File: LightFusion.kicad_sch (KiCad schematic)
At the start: 28 parts, among them IC2 ADS1291IPBSR, U1 BMD-350-A-R

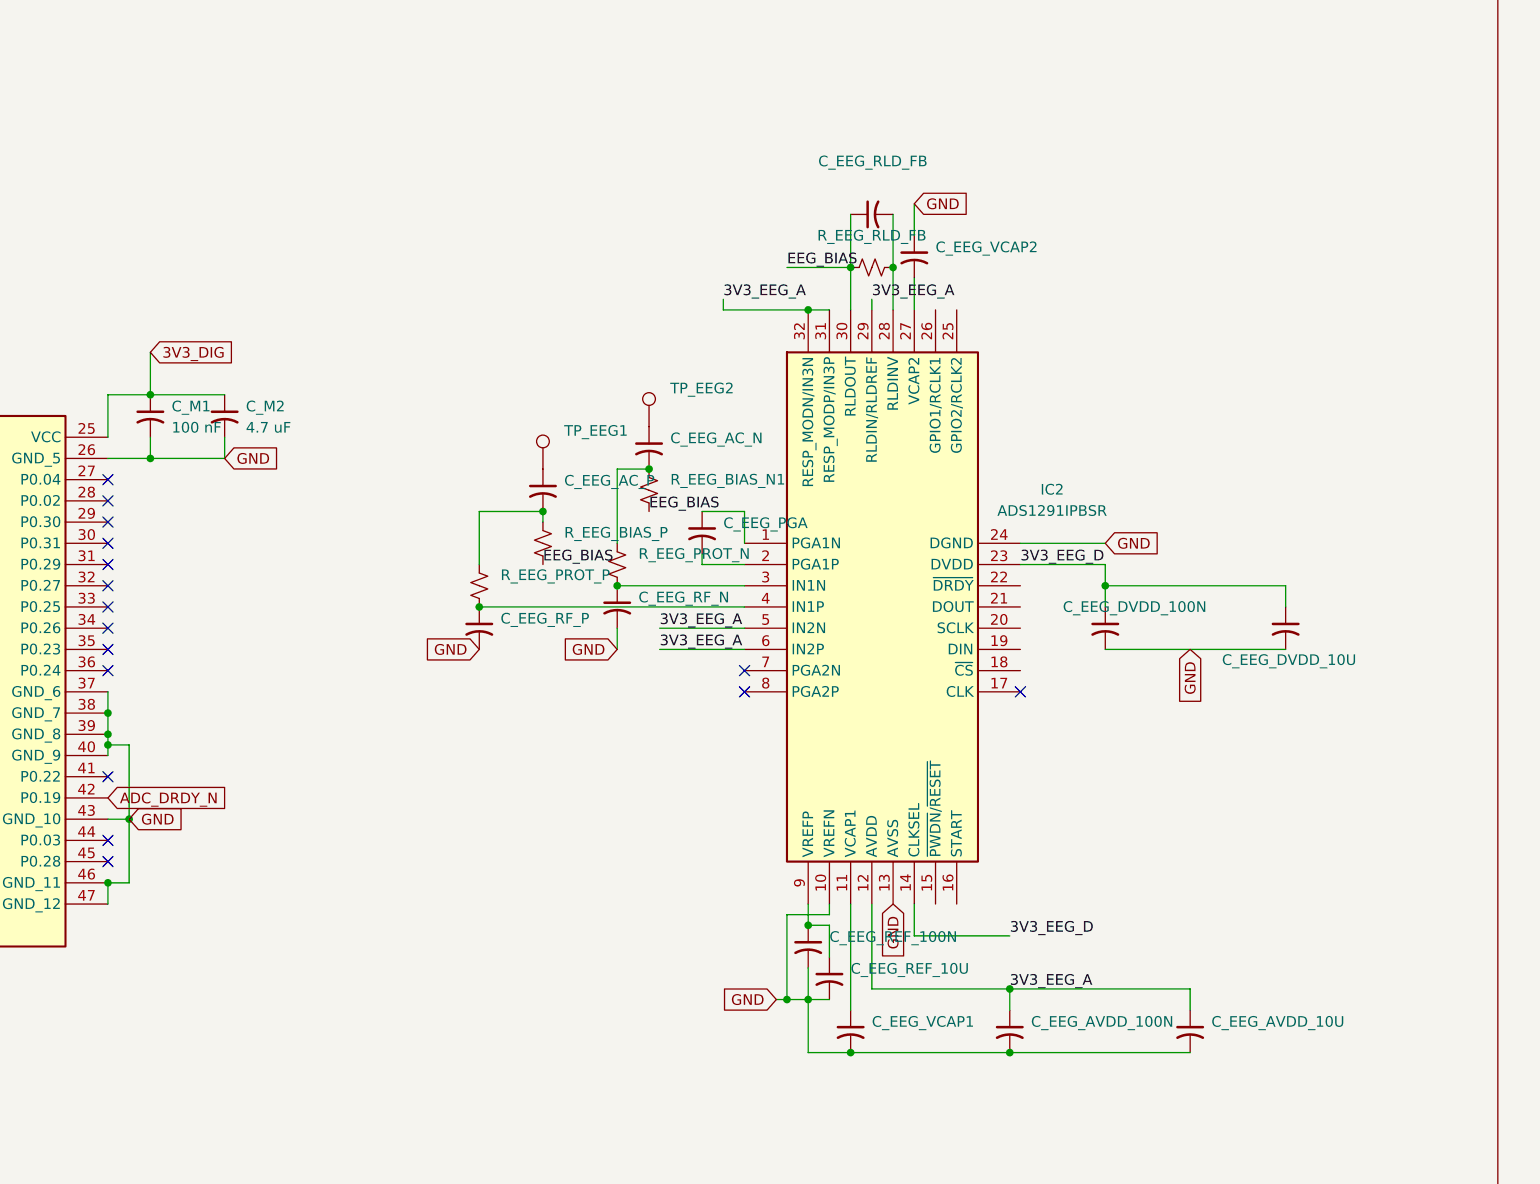
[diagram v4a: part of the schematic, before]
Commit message: eeg part refactored
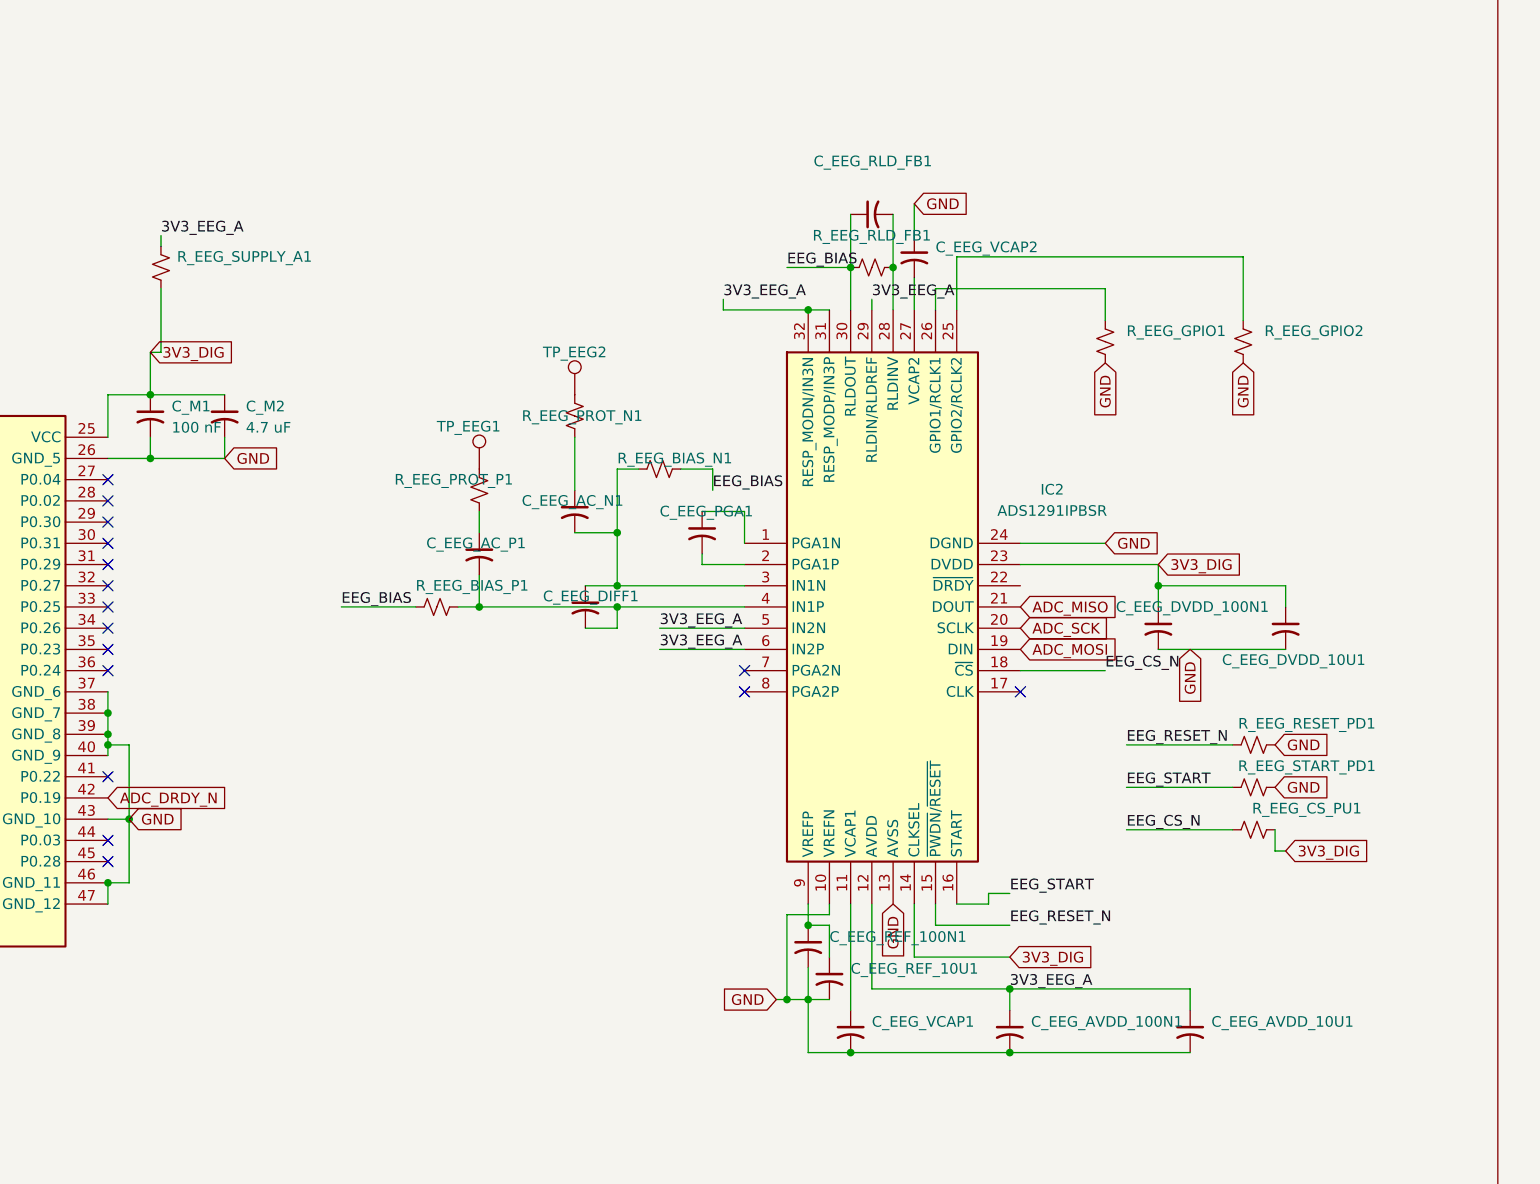
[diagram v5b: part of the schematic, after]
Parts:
- removed C_EEG_RF_P: 47 pF, symbol C_Small_US:C_Small_US
- added R_EEG_CS_PU1, R_EEG_RESET_PD1, R_EEG_START_PD1: 100 kΩ, symbol R_Small_US:R_Small_US
- added R_EEG_GPIO1, R_EEG_GPIO2: 10 kΩ, symbol R_Small_US:R_Small_US
- added R_EEG_SUPPLY_A1: 10 Ω, symbol R_Small_US:R_Small_US
- C_EEG_DIFF1: renamed from C_EEG_RF_N; value 47 pF -> 2.2 nF
- TP_EEG1, TP_EEG2: footprint (none) -> LightFusion:TestPoint_Plated_Hole_D3.0mm
- renumbered C_EEG_AC_N to C_EEG_AC_N1, C_EEG_AC_P to C_EEG_AC_P1, C_EEG_AVDD_100N to C_EEG_AVDD_100N1, C_EEG_AVDD_10U to C_EEG_AVDD_10U1, C_EEG_DVDD_100N to C_EEG_DVDD_100N1, C_EEG_DVDD_10U to C_EEG_DVDD_10U1, C_EEG_PGA to C_EEG_PGA1, C_EEG_REF_100N to C_EEG_REF_100N1, C_EEG_REF_10U to C_EEG_REF_10U1, C_EEG_RLD_FB to C_EEG_RLD_FB1, R_EEG_BIAS_P to R_EEG_BIAS_P1, R_EEG_PROT_N to R_EEG_PROT_N1, R_EEG_PROT_P to R_EEG_PROT_P1, R_EEG_RLD_FB to R_EEG_RLD_FB1
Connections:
- net 3V3_EEG_D is gone; now on net 3V3_DIG: C_EEG_DVDD_100N1.1, C_EEG_DVDD_10U1.1, IC2.14 (CLKSEL), IC2.23 (DVDD)
- net 3V3_DIG: now also R_EEG_CS_PU1.2, R_EEG_SUPPLY_A1.2
- net 3V3_EEG_A: now also R_EEG_SUPPLY_A1.1
- net ADC_MISO: now also IC2.21 (DOUT)
- net ADC_MOSI: now also IC2.19 (DIN)
- net ADC_SCK: now also IC2.20 (SCLK)
- net EEG_BIAS: now also R_EEG_BIAS_N1.1; no longer R_EEG_BIAS_N1.2
- net GND: now also R_EEG_GPIO1.2, R_EEG_GPIO2.2, R_EEG_RESET_PD1.2, R_EEG_START_PD1.2; no longer C_EEG_DIFF1.2
- net at C_EEG_DIFF1.1, IC2.3 (IN1N): now also C_EEG_AC_N1.2, R_EEG_BIAS_N1.2; no longer R_EEG_PROT_N1.2
- net at TP_EEG1.1: now also R_EEG_PROT_P1.1; no longer C_EEG_AC_P1.1
- net at IC2.4 (IN1P): now also C_EEG_AC_P1.2, C_EEG_DIFF1.2, R_EEG_BIAS_P1.1; no longer R_EEG_PROT_P1.2
- net at TP_EEG2.1: now also R_EEG_PROT_N1.1; no longer C_EEG_AC_N1.1
- net EEG_RESET_N: now reaches IC2.15 (~{PWDN}/~{RESET})
- net EEG_RESET_N: now also R_EEG_RESET_PD1.1
- net EEG_START: now reaches IC2.16 (START)
- net EEG_START: now also R_EEG_START_PD1.1
- net EEG_CS_N: now reaches IC2.18 (~{CS})
- net EEG_CS_N: now also R_EEG_CS_PU1.1
- net at IC2.25 (GPIO2/RCLK2): now also R_EEG_GPIO2.1
- net at IC2.26 (GPIO1/RCLK1): now also R_EEG_GPIO1.1
- new net: C_EEG_AC_N1.1, R_EEG_PROT_N1.2
- new net: C_EEG_AC_P1.1, R_EEG_PROT_P1.2
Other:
- moved on the sheet: C_EEG_AC_N1, C_EEG_AC_P1, C_EEG_DIFF1, C_EEG_DVDD_100N1, R_EEG_BIAS_N1, R_EEG_BIAS_P1, R_EEG_PROT_N1, R_EEG_PROT_P1, TP_EEG1, TP_EEG2

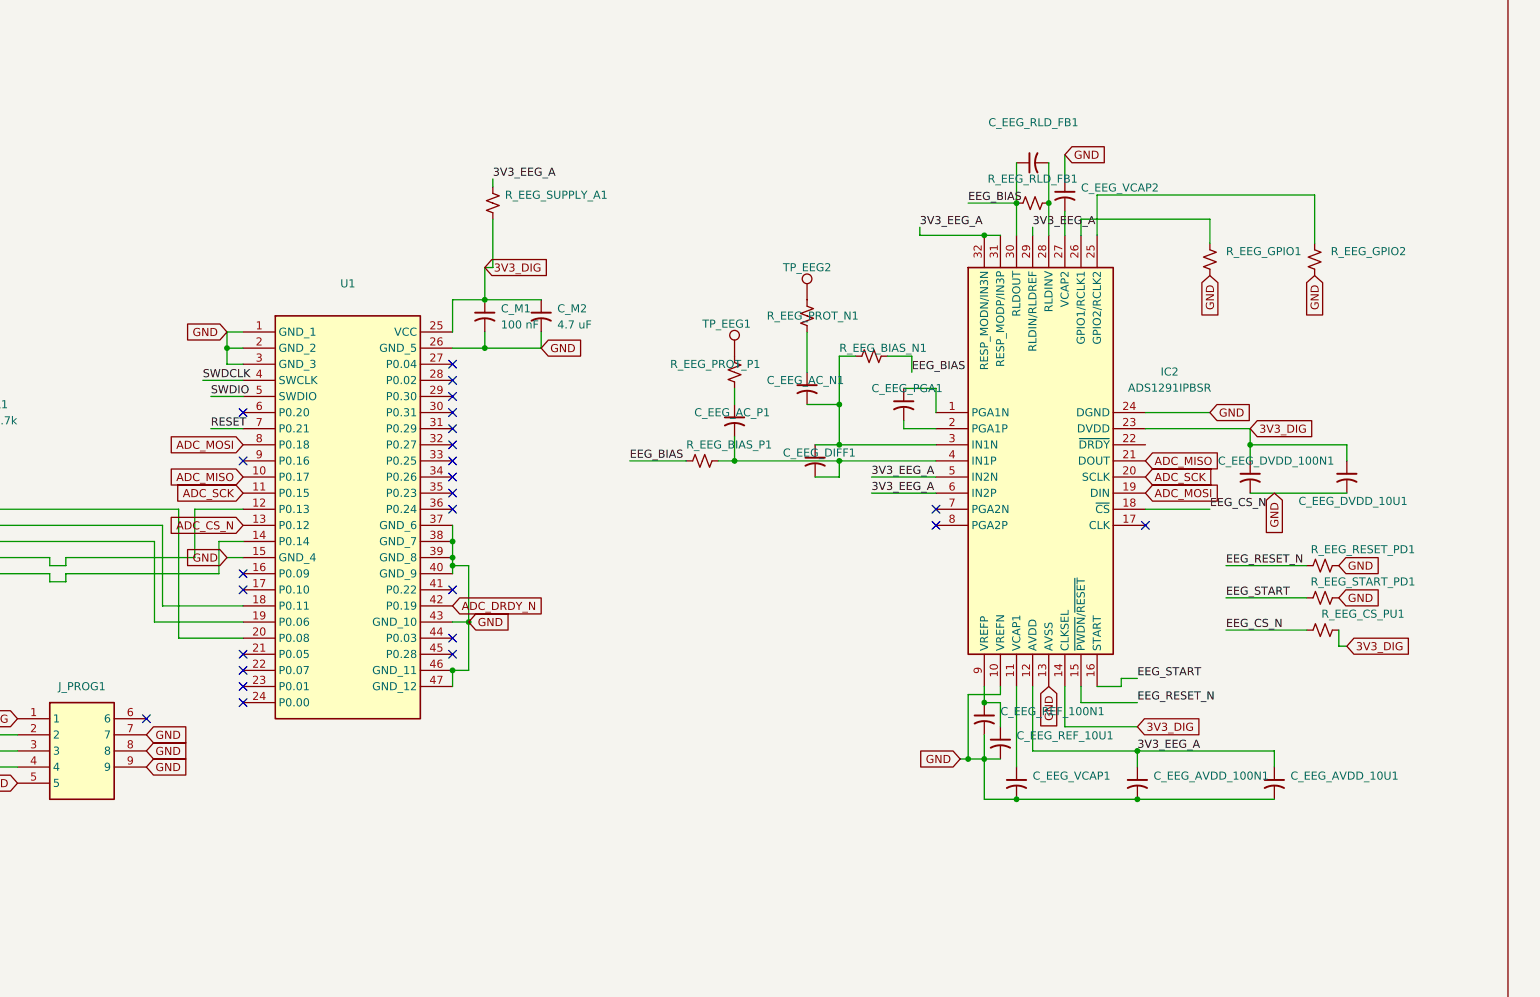
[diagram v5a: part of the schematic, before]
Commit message: eeg part refactored electrodes
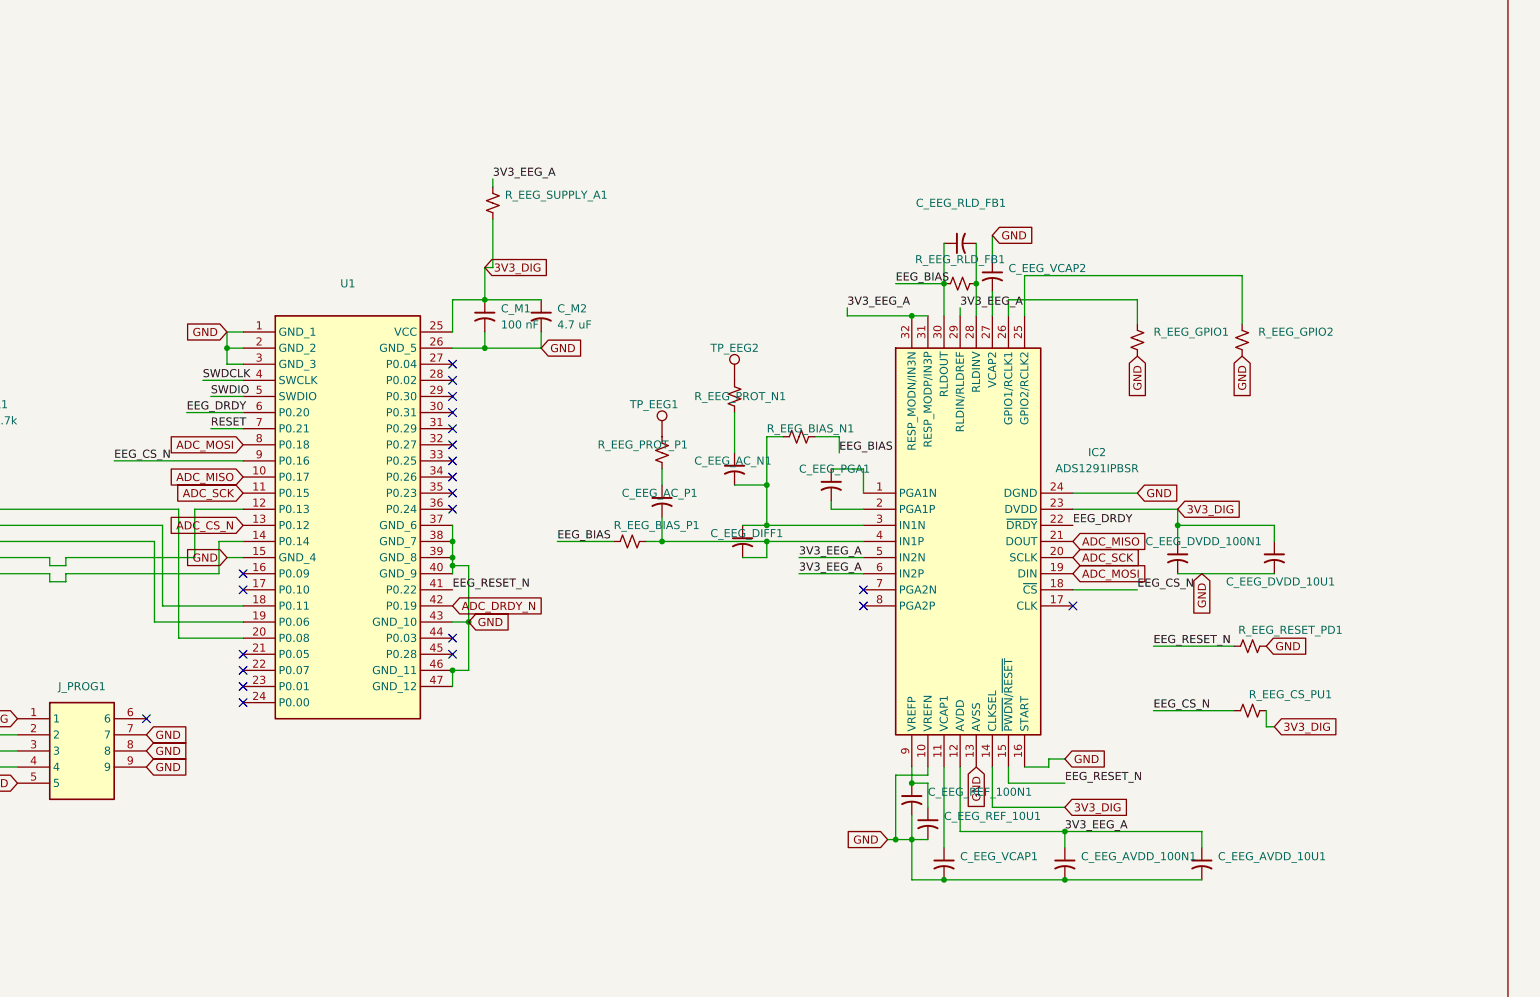
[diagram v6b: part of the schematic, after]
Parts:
- removed R_EEG_START_PD1: 100 kΩ, symbol R_Small_US:R_Small_US
- C_EEG_AC_N1, C_EEG_AC_P1, C_EEG_AVDD_100N1, C_EEG_DVDD_100N1, C_EEG_REF_100N1: footprint (none) -> LightFusion:C_0603_1608Metric
- C_EEG_AVDD_10U1, C_EEG_DVDD_10U1, C_EEG_REF_10U1: footprint (none) -> LightFusion:C_0805_2012Metric
- C_EEG_DIFF1, C_EEG_RLD_FB1: footprint (none) -> LightFusion:C_0402_1005Metric
- C_EEG_VCAP1, C_EEG_VCAP2: footprint (none) -> LightFusion:CAPPC2012X90N
- R_EEG_BIAS_N1, R_EEG_BIAS_P1, R_EEG_CS_PU1, R_EEG_GPIO1, R_EEG_GPIO2, R_EEG_PROT_N1, R_EEG_PROT_P1, R_EEG_RESET_PD1, R_EEG_RLD_FB1, R_EEG_SUPPLY_A1: footprint (none) -> LightFusion:R_0603_1608Metric
- TP_EEG1, TP_EEG2: footprint LightFusion:TestPoint_Plated_Hole_D3.0mm -> LightFusion:TestPoint_Pad_D3.0mm
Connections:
- net EEG_START is gone; now on net GND: IC2.16 (START)
- net EEG_CS_N: now also U1.9 (P0.16)
- net EEG_RESET_N: now also U1.41 (P0.22)
- net EEG_DRDY: now reaches U1.6 (P0.20)
- net EEG_DRDY: now also IC2.22 (~{DRDY})
- no-connect marks 25 -> 22
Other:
- moved on the sheet: C_EEG_AC_N1, C_EEG_AC_P1, C_EEG_AVDD_100N1, C_EEG_AVDD_10U1, C_EEG_DIFF1, C_EEG_DVDD_100N1, C_EEG_DVDD_10U1, C_EEG_PGA1, C_EEG_REF_100N1, C_EEG_REF_10U1, C_EEG_RLD_FB1, C_EEG_VCAP1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

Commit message: added pogo electrodes
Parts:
- TP_EEG1, TP_EEG2: footprint LightFusion:TestPoint_Pad_D3.0mm -> LightFusion:MILL-MAX_0906-0-15-20-76-14-11-0
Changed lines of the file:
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@@
 			)
 		)
-		(property "Footprint" "LightFusion:TestPoint_Pad_D3.0mm"
+		(property "Footprint" "LightFusion:MILL-MAX_0906-0-15-20-76-14-11-0"
 			(at 171.45 82.55 0)
 			(hide yes)
@@
 			)
 		)
-		(property "Footprint" "LightFusion:TestPoint_Pad_D3.0mm"
+		(property "Footprint" "LightFusion:MILL-MAX_0906-0-15-20-76-14-11-0"
 			(at 182.88 73.66 0)
 			(hide yes)

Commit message: eeg 3rd electrode added
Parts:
- removed IC2: ADS1291IPBSR, LightFusion:ADS1291IPBSR, symbol ADS1291IPBSR:ADS1291IPBSR
- added C_EEG_AC_N2, C_EEG_AC_P2: 47 nF, LightFusion:C_0603_1608Metric, symbol C_Small_US:C_Small_US
- added C_EEG_DIFF2: 2.2 nF, LightFusion:C_0402_1005Metric, symbol C_Small_US:C_Small_US
- added C_EEG_PGA2: 4.7 nF, LightFusion:C_0402_1005Metric, symbol C_Small_US:C_Small_US
- added IC2: ADS1292IPBSR, LightFusion:ADS1292IPBSR, symbol ADS1292IPBSR:ADS1292IPBSR
- added R_EEG_BIAS_N2, R_EEG_BIAS_P2: 22 MΩ, LightFusion:R_0603_1608Metric, symbol R_Small_US:R_Small_US
- added R_EEG_PROT_N2, R_EEG_PROT_P2: 51 kΩ, LightFusion:R_0603_1608Metric, symbol R_Small_US:R_Small_US
- added TP_EEG3: TestPoint, LightFusion:MILL-MAX_0906-0-15-20-76-14-11-0, symbol TestPoint:TestPoint
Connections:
- net 3V3_DIG: now also IC2.14 (CLKSEL), IC2.23 (DVDD)
- net 3V3_EEG_A: now also IC2.12 (AVDD), IC2.29 (RLDIN/RLDREF), IC2.32 (RESP_MODN/IN3N)
- net ADC_MISO: now also IC2.21 (DOUT)
- net ADC_MOSI: now also IC2.19 (DIN)
- net ADC_SCK: now also IC2.20 (SCLK)
- net EEG_BIAS: now also IC2.30 (RLDOUT), R_EEG_BIAS_N2.2, R_EEG_BIAS_P2.2
- net EEG_CS_N: now also IC2.18 (~{CS})
- net EEG_DRDY: now also IC2.22 (~{DRDY})
- net EEG_RESET_N: now also IC2.15 (~{PWDN}/~{RESET})
- net GND: now also IC2.10 (VREFN), IC2.13 (AVSS), IC2.16 (START), IC2.24 (DGND)
- net at C_EEG_RLD_FB1.2, R_EEG_RLD_FB1.2: now also IC2.28 (RLDINV)
- net at C_EEG_AC_N1.2, C_EEG_DIFF1.1, R_EEG_BIAS_N1.2: now also IC2.3 (IN1N)
- net at C_EEG_AC_P1.2, C_EEG_DIFF1.2, R_EEG_BIAS_P1.1: now also IC2.4 (IN1P)
- net at C_EEG_VCAP1.1: now also IC2.11 (VCAP1)
- net at C_EEG_REF_100N1.1, C_EEG_REF_10U1.1: now also IC2.9 (VREFP)
- net at C_EEG_PGA1.1: now also IC2.1 (PGA1N)
- net at C_EEG_PGA1.2: now also IC2.2 (PGA1P)
- net at R_EEG_GPIO2.1: now also IC2.25 (GPIO2/RCLK2)
- net at R_EEG_GPIO1.1: now also IC2.26 (GPIO1/RCLK1)
- net at C_EEG_VCAP2.2: now also IC2.27 (VCAP2)
- new net: C_EEG_PGA2.1, IC2.7 (PGA2N)
- new net: C_EEG_PGA2.2, IC2.8 (PGA2P)
- new net: C_EEG_AC_P2.2, C_EEG_DIFF2.1, IC2.6 (IN2P), R_EEG_BIAS_P2.1
- new net: C_EEG_AC_N2.2, C_EEG_DIFF2.2, IC2.5 (IN2N), R_EEG_BIAS_N2.1
- new net: C_EEG_AC_P2.1, R_EEG_PROT_P2.2
- new net: C_EEG_AC_N2.1, R_EEG_PROT_N2.2
- new net: R_EEG_PROT_N2.1, R_EEG_PROT_P2.1, TP_EEG3.1
- no-connect marks 22 -> 20
